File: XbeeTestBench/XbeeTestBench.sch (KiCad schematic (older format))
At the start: 12 parts, among them J1 Conn_01x02, J2 Conn_01x06, J3 Conn_01x15, J4 Conn_01x15, J5 Conn_01x08, J6 Conn_01x02, U1 Xbee802.15.4

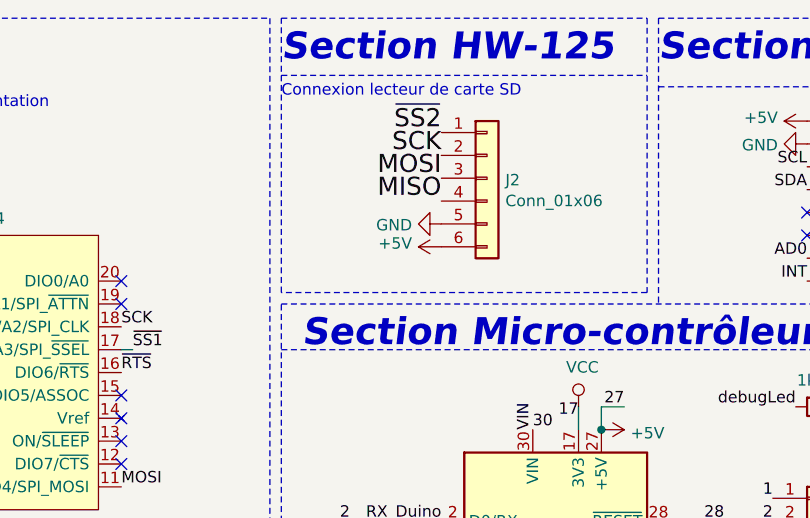
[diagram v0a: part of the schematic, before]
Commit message: MàJ des test bench, ajout des projets ElecExterne et ElecInterne
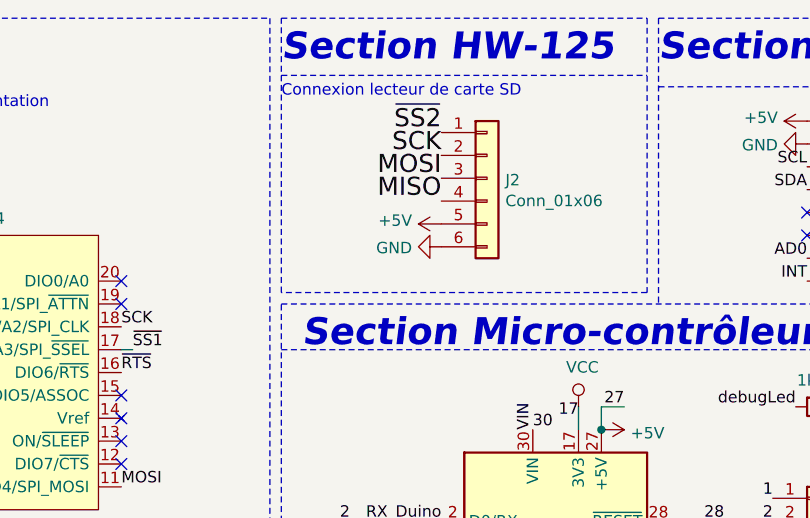
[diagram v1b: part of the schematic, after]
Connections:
- net +5V: now also J2.5 (Pin_5); no longer J2.6 (Pin_6)
- net GND: now also J2.6 (Pin_6); no longer J2.5 (Pin_5)
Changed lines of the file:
@@
 L power:GND #PWR08
 U 1 1 5DE82655
-P 3850 1400
-F 0 "#PWR08" H 3850 1150 50  0001 C CNN
-F 1 "GND" V 3855 1272 50  0000 R CNN
-F 2 "" H 3850 1400 50  0001 C CNN
-F 3 "" H 3850 1400 50  0001 C CNN
-	1    3850 1400
+P 3850 1500
+F 0 "#PWR08" H 3850 1250 50  0001 C CNN
+F 1 "GND" V 3855 1372 50  0000 R CNN
+F 2 "" H 3850 1500 50  0001 C CNN
+F 3 "" H 3850 1500 50  0001 C CNN
+	1    3850 1500
 	0    1    1    0
 $EndComp
@@
 L power:+5V #PWR09
 U 1 1 5DE82851
-P 3850 1500
-F 0 "#PWR09" H 3850 1350 50  0001 C CNN
-F 1 "+5V" V 3865 1628 50  0000 L CNN
-F 2 "" H 3850 1500 50  0001 C CNN
-F 3 "" H 3850 1500 50  0001 C CNN
-	1    3850 1500
+P 3850 1400
+F 0 "#PWR09" H 3850 1250 50  0001 C CNN
+F 1 "+5V" V 3865 1528 50  0000 L CNN
+F 2 "" H 3850 1400 50  0001 C CNN
+F 3 "" H 3850 1400 50  0001 C CNN
+	1    3850 1400
 	0    -1   -1   0
 $EndComp
